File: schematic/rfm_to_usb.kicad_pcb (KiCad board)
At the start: 2 copper layers, 16 parts, among them J1 USB_A, J2 ant, U1 STM32F103C8, U2 XC6206-33, X1 SWD_CON

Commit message: err in pcb
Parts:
- moved R4 8.69 mm to (58.5, 49.7), turned to 90 degrees
- moved C6 0.54 mm to (66.5, 35.3)
- moved R2 0.15 mm to (61.6, 49.7)
- moved R3 0.15 mm to (60.0, 49.7)
- moved X1 0.13 mm to (64.5, 50.0)
- moved J2 0.08 mm to (54.6, 48.5)
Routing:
- net +3V3: track 80.5 -> 84.9 mm
- net Net-(J1-Pad2): track 5.88 -> 7.05 mm
- net /SCK: track 5.17 -> 6.31 mm
- net /MISO: track 23.7 -> 22.6 mm
- net /NSS: track 6.28 -> 7.27 mm
- net /DIO0: track 18.0 -> 17.0 mm
- net Net-(J1-Pad3): track 7.87 -> 6.94 mm
- net Net-(R3-Pad2): track 9.50 -> 8.76 mm
- net /DIO1: track 20.4 -> 21.1 mm
- net Net-(D1-Pad12): track 18.1 -> 18.8 mm

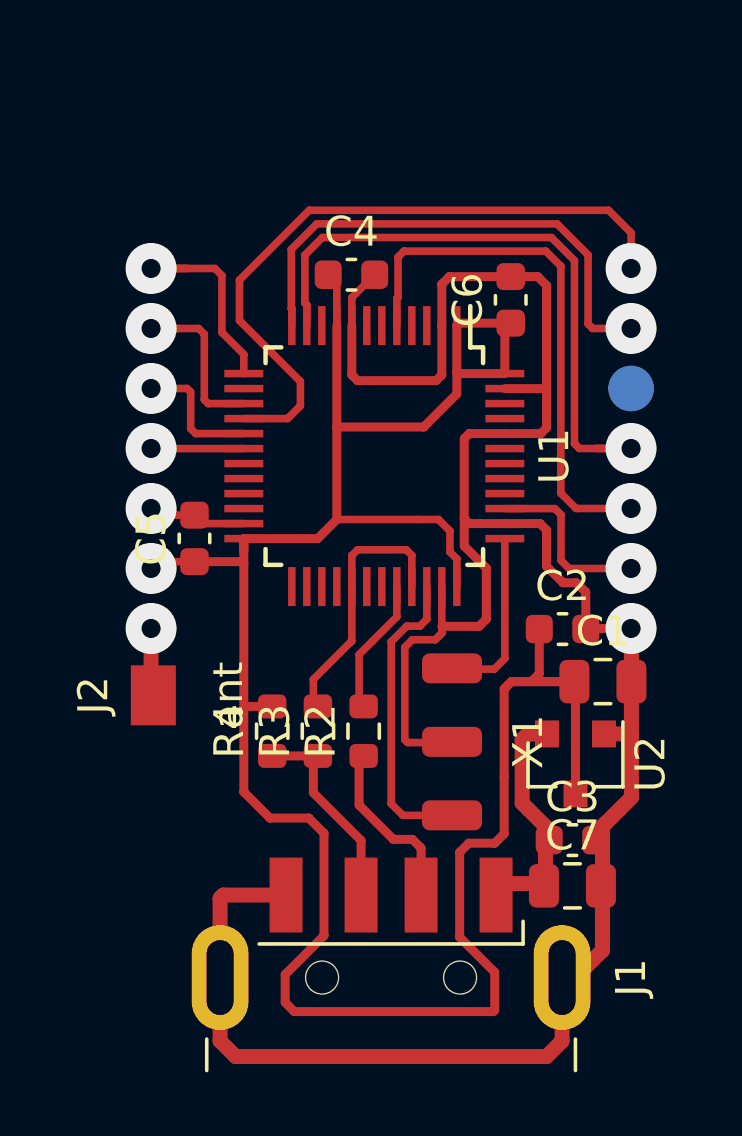
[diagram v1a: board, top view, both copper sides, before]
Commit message: add uart, 2.8 mm lenght
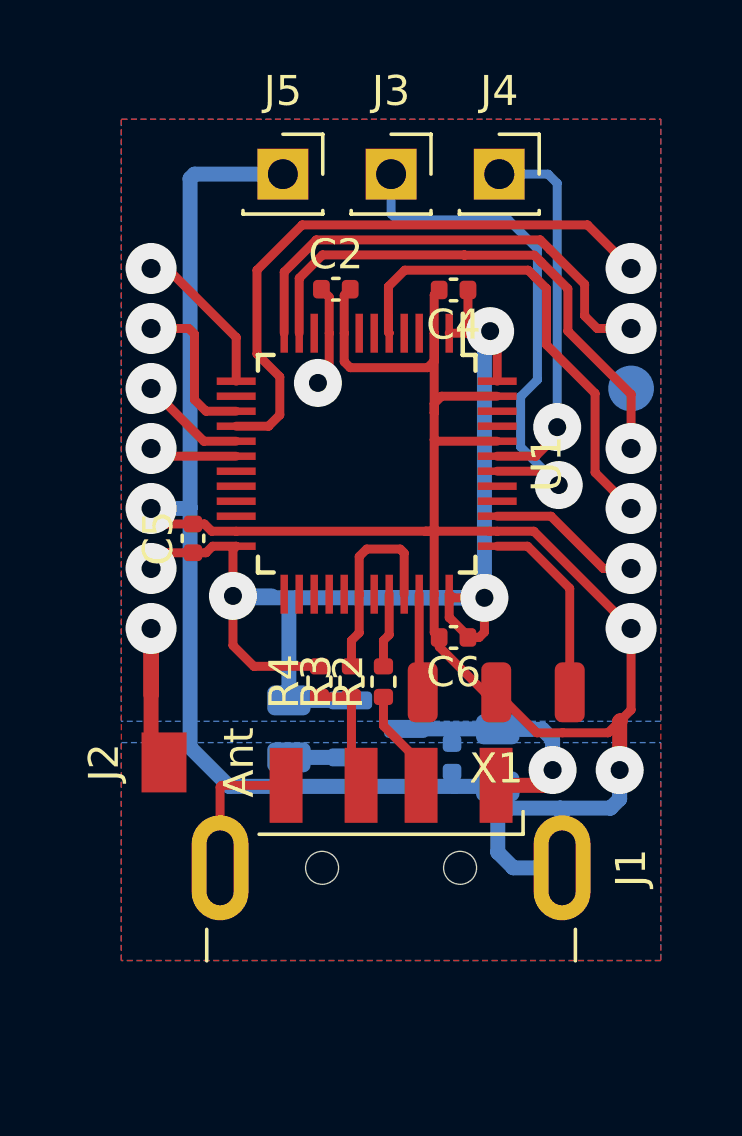
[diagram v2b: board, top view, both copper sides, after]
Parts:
- added J3: UART_TX, Connector_PinSocket_2.54mm:PinSocket_1x01_P2.54mm_Vertical, F.Cu at (62.5, 31.1)
- added J4: UART_RX, Connector_PinSocket_2.54mm:PinSocket_1x01_P2.54mm_Vertical, F.Cu at (66.1, 31.1)
- added J5: GND, Connector_PinSocket_2.54mm:PinSocket_1x01_P2.54mm_Vertical, F.Cu at (58.9, 31.1)
- C1, C7, U2: moved to B.Cu
- C2, C4, C5, C6: footprint Capacitor_SMD:C_0603_1608Metric -> Capacitor_SMD:C_0402_1005Metric
- C3: footprint Capacitor_SMD:C_0603_1608Metric -> Capacitor_SMD:C_0402_1005Metric; moved to B.Cu
- J2: value ant -> Ant
- R2, R3, R4: footprint Resistor_SMD:R_0603_1608Metric -> Resistor_SMD:R_0402_1005Metric
- moved C2 13.6 mm to (60.6, 34.9)
- moved C6 11.4 mm to (64.6, 46.5), turned to 180 degrees
- moved C1 10.6 mm to (59.1, 49.6), turned to 270 degrees
- moved U2 6.68 mm to (62.1, 49.6), turned to 0 degrees
- moved C7 4.94 mm to (66.0, 50.5), turned to 270 degrees
- moved C3 4.86 mm to (64.5, 50.5), turned to 270 degrees
- moved J1 3.66 mm to (62.5, 61.1)
- moved C4 3.44 mm to (64.6, 35.0), turned to 180 degrees
- moved R4 2.28 mm to (60.1, 48.0)
- moved J2 2.26 mm to (54.9, 50.7)
- moved X1 2.21 mm to (66.0, 48.4), turned to 180 degrees
- moved R3 1.99 mm to (61.2, 48.0)
- moved R2 1.78 mm to (62.2, 48.0)
- moved U1 0.36 mm to (61.7, 40.7)
- moved C5 0.05 mm to (55.9, 43.2)
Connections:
- U1 pad 29: Net-(R3-Pad2) -> Net-(U1-Pad29)
- U1 pad 30: Net-(U1-Pad30) -> Net-(R3-Pad2)
- U2 pad 2: +5V -> +3V3
- U2 pad 3: +3V3 -> +5V
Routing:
- net +3V3: track 84.9 -> 51.2 mm, vias 1 -> 5
- net GND: track 87.7 -> 108.2 mm, vias 2 -> 3
- net Net-(J3-Pad1): track 0.00 -> 18.5 mm, vias 0 -> 1
- net Net-(J4-Pad1): track 0.00 -> 13.0 mm, vias 0 -> 1
- net Net-(U1-Pad34): track 10.2 -> 3.32 mm
- net Net-(D1-Pad1): track 2.23 -> 6.87 mm
- net Net-(J1-Pad2): track 7.05 -> 3.47 mm
- net /DIO1: track 21.1 -> 18.0 mm
- net Net-(D1-Pad12): track 18.8 -> 15.8 mm
- net Net-(J1-Pad3): track 6.94 -> 4.22 mm
- net /MISO: track 22.6 -> 20.4 mm
- net Net-(R2-Pad2): track 4.52 -> 2.48 mm
- net /NSS: track 7.27 -> 5.25 mm
- net Net-(R3-Pad2): track 8.76 -> 6.80 mm
- net /DIO0: track 17.0 -> 15.9 mm
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- added copper zone on B.Cu, net +3V3
- added copper zone on B.Cu, net GND
- added copper zone on F.Cu, net GND
